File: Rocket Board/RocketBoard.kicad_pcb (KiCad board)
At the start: 2 copper layers, 52 parts, among them P1 PA_8, P10 PB_5, P11 PC_9, P12 PC_8, P13 PC_0, P14 PC_1, P15 PC_2, P16 PC_3, P17 CONN_01X04, P18 I2C, P19 Power, P2 PA_9, P3 PA_10, P4 PA_11, P5 PB_2, P6 PB_1, P7 PC_5, P8 PC_4, P9 PB_4, SW1 SPST, U1 STM32F401RCT6, U2 LD1117S33TR, Y1 25MHz

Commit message: Partial Layout of Board
Started the board layout process
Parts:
- added REF**: MountingHole_3.5mm_Pad, Mounting_Holes:MountingHole_3.5mm_Pad, F.Cu at (105.7, 100.3)
- added REF**: MountingHole_2.5mm_Pad, Mounting_Holes:MountingHole_2.5mm_Pad, F.Cu at (103.9, 120.9)
- C1, C10, C2, C3, C4, C5, C6, C7, C9: moved to B.Cu
- SWD: renamed from P17; value CONN_01X04 -> SWD
- Status 1: renamed from D2
- Status 2: renamed from D3
- moved P3 139.7 mm to (176.5, 95.2), turned to 90 degrees
- moved P15 131.8 mm to (176.5, 107.4), turned to 90 degrees
- moved P14 130.7 mm to (176.5, 104.4), turned to 90 degrees
- moved P13 129.7 mm to (176.5, 101.3), turned to 90 degrees
- moved P4 128.7 mm to (176.5, 98.3), turned to 90 degrees
- moved P1 127.3 mm to (176.5, 89.2), turned to 90 degrees
- moved P12 125.5 mm to (176.5, 86.1), turned to 90 degrees
- moved P11 124.9 mm to (176.5, 83.1), turned to 90 degrees
- moved P10 124.3 mm to (176.5, 80.0), turned to 90 degrees
- moved RP1 119.6 mm to (168.4, 93.7)
- moved C7 109.7 mm to (153.7, 91.7), turned to 90 degrees
- moved C2 99.8 mm to (143.0, 103.9)
- moved C4 99.8 mm to (142.0, 92.5), turned to 90 degrees
- moved C3 97.7 mm to (143.5, 98.0), turned to 90 degrees
- moved R4 96.8 mm to (148.1, 81.5)
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- renumbered D1 to PWR
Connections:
- RP1 pad 1: /PA_8 -> /PA_11
- RP1 pad 2: /PA_9 -> /PA_10
- RP1 pad 3: /PA_10 -> /PA_9
- RP1 pad 4: /PA_11 -> /PA_8
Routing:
- net GND: track 0.00 -> 43.7 mm, vias 0 -> 3
- net +3V3: track 0.00 -> 21.9 mm, vias 0 -> 3
- net /NRST: track 0.00 -> 10.8 mm
- net Net-(D3-Pad2): track 0.00 -> 9.67 mm
- net Net-(D2-Pad2): track 0.00 -> 9.67 mm
- net /PC_4: track 0.00 -> 9.41 mm
- net /OSC2: track 0.00 -> 9.11 mm, vias 0 -> 2
- net /PC_5: track 0.00 -> 8.77 mm
- net /PB_1: track 0.00 -> 8.19 mm
- net /PA_1: track 0.00 -> 7.99 mm
- net +12V: track 0.00 -> 7.91 mm
- net /PB_2: track 0.00 -> 7.84 mm
- net /OSC1: track 0.00 -> 7.74 mm
- net Net-(C15-Pad2): track 0.00 -> 6.19 mm
- net /PA_0: track 0.00 -> 5.78 mm
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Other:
- board outline added: 64.5 x 40.9 mm
- rule trace_min: 0.2 -> 0.1

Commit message: Finish Layout
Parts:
- removed the REF** at (105.7, 100.3)
- added MAV3: MAVRIC, Labels:MAVRIC, B.Cu at (132.8, 91.7)
- R3, R4: moved to B.Cu
- moved REF** 50.7 mm to (153.7, 111.5)
- moved R3 7.45 mm to (140.9, 81.5), turned to 270 degrees
- moved P1 6.87 mm to (169.7, 89.5)
- moved P12 6.87 mm to (169.7, 86.5)
- moved P15 6.87 mm to (169.7, 107.8)
- moved P16 6.87 mm to (169.7, 110.8)
- moved P10 6.87 mm to (169.7, 80.4)
- moved P11 6.87 mm to (169.7, 83.4)
- moved P13 6.87 mm to (169.7, 101.7)
- moved P14 6.87 mm to (169.7, 104.7)
- moved P2 6.87 mm to (169.7, 92.6)
- moved P3 6.87 mm to (169.7, 95.6)
- moved P4 6.87 mm to (169.7, 98.7)
- moved P9 6.87 mm to (169.7, 77.3)
- moved RP1 6.87 mm to (161.5, 94.1)
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- renumbered P18 to I2C
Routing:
- net GND: track 43.7 -> 93.0 mm, vias 3 -> 17
- net /PC_3: track 0.00 -> 29.7 mm, vias 0 -> 2
- net /PC_2: track 0.00 -> 28.5 mm, vias 0 -> 2
- net /PC_1: track 0.00 -> 26.9 mm, vias 0 -> 2
- net Net-(P8-Pad1): track 0.00 -> 26.5 mm
- net /PB_5: track 0.00 -> 26.1 mm
- net /PC_0: track 0.00 -> 25.9 mm, vias 0 -> 2
- net Net-(P7-Pad1): track 0.00 -> 25.7 mm
- net /PC_8: track 0.00 -> 24.2 mm, vias 0 -> 2
- net /PC_9: track 0.00 -> 23.9 mm, vias 0 -> 2
- net Net-(P6-Pad1): track 0.00 -> 23.6 mm
- net /SCL_1: track 0.00 -> 23.0 mm, vias 0 -> 1
- net +3V3: track 21.9 -> 43.5 mm, vias 3 -> 5
- net /NRST: track 10.8 -> 31.7 mm, vias 0 -> 1
- net /SDA_1: track 0.00 -> 20.4 mm, vias 0 -> 1
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- added copper zone on F.Cu, net +3V3
- added copper zone on B.Cu, net GND
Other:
- board size 64.5 x 40.9 mm -> 58.5 x 40.9 mm
- board text added: "M A V R I C Main Board"

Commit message: Fix analog input, Add 2 UART ports, changed PWM1/3 to PWM1/3N
Removed the series resistors for analog inputs, added pinouts for
UART1,2.   Changed PWM 1/3 tp PWM 1/3N to free up RX1 pin
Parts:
- removed P13: PC_0, Pin_Headers:Pin_Header_Straight_1x02
- removed P14: PC_1, Pin_Headers:Pin_Header_Straight_1x02
- removed P15: PC_2, Pin_Headers:Pin_Header_Straight_1x02
- removed P16: PC_3, Pin_Headers:Pin_Header_Straight_1x02
- removed REF**: MountingHole_2.5mm_Pad, Mounting_Holes:MountingHole_2.5mm_Pad
- removed RP4: 220 4pack, Resistors_SMD:R_Array_Convex_4x1206
- added PC0: PC_0, Pin_Headers:Pin_Header_Straight_1x02, F.Cu at (169.7, 101.8)
- added PC1: PC_1, Pin_Headers:Pin_Header_Straight_1x02, F.Cu at (169.7, 104.9)
- added PC2: PC_2, Pin_Headers:Pin_Header_Straight_1x02, F.Cu at (169.7, 108.0)
- added PC3: PC_3, Pin_Headers:Pin_Header_Straight_1x02, F.Cu at (169.7, 111.0)
- added UART1: UART1, Pin_Headers:Pin_Header_Straight_1x02, F.Cu at (153.8, 110.8)
- added UART2: UART2, Pin_Headers:Pin_Header_Straight_1x02, F.Cu at (159.4, 110.9)
- renumbered P3 to PA10, P4 to PA11, P1 to PA8, P2 to PA9, P6 to PB1, P5 to PB2, P9 to PB4, P10 to PB5, P8 to PC4, P7 to PC5, P12 to PC8, P11 to PC9
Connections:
- RP1 pad 1: /PA_11 -> /PB_15
- RP1 pad 2: /PA_10 -> /PA_11
- U1 pad 16: GND -> /TX2
- U1 pad 17: GND -> /RX2
- U1 pad 36: GND -> /PB_15
- U1 pad 43: /PA_10 -> /RX1
- U1 pad 58: GND -> /TX1
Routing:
- net /RX2: track 0.00 -> 37.9 mm
- net /TX2: track 0.00 -> 37.8 mm
- net /TX1: track 0.00 -> 26.3 mm
- net +3V3: track 43.5 -> 65.3 mm, vias 5 -> 9
- net /RX1: track 0.00 -> 17.9 mm
- net /PB_15: track 0.00 -> 17.8 mm
- net /PC_3: track 29.7 -> 40.4 mm
- net (no net): track 0.00 -> 10.2 mm, vias 0 -> 2
- net /PC_2: track 28.5 -> 37.7 mm
- net /PA_10: track 8.79 -> 0.00 mm
- net /PC_1: track 26.9 -> 35.1 mm
- net /PC_0: track 25.9 -> 33.7 mm
- net Net-(P13-Pad1): track 7.69 -> 0.00 mm
- net Net-(P16-Pad1): track 7.69 -> 0.00 mm
- net Net-(P15-Pad1): track 6.99 -> 0.00 mm
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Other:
- board text added: "Analog"
- board text added: "GND"
- board text added: "M A V R I C Danny Mallek 2016"
- board text added: "Main Board Rev2.0"
- board text removed: "M A V R I C Main Board"

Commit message: Fix power distribution issues on main board, initial soil board commit
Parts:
- renumbered P19 to PWR
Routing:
- net +3V3: track 65.3 -> 91.7 mm, vias 9 -> 12
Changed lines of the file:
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@@
   (general
     (links 142)
-    (no_connects 8)
+    (no_connects 5)
     (area 116.764999 74.346999 175.385801 115.391001)
     (thickness 1.6)
     (drawings 15)
-    (tracks 511)
+    (tracks 533)
     (zones 0)
     (modules 54)
@@
     (descr "Through hole pin header")
     (tags "pin header")
-    (fp_text reference P19 (at 0.0508 4.9784) (layer F.SilkS)
+    (fp_text reference PWR (at 0.0508 4.9784) (layer F.SilkS)
       (effects (font (size 1 1) (thickness 0.15)))
     )
@@
   (segment (start 145.4404 113.6396) (end 144.4244 112.6236) (width 0.4) (layer B.Cu) (net 0))
   (via (at 145.4404 113.6396) (size 0.8) (drill 0.6) (layers F.Cu B.Cu) (net 0))
+  (segment (start 127.762 84.836) (end 129.54 86.614) (width 0.75) (layer F.Cu) (net 1))
+  (via (at 129.54 86.614) (size 0.8) (drill 0.6) (layers F.Cu B.Cu) (net 1))
+  (segment (start 127.73 84.614) (end 129.54 82.804) (width 0.75) (layer F.Cu) (net 1))
+  (via (at 129.54 82.804) (size 0.8) (drill 0.6) (layers F.Cu B.Cu) (net 1))
   (segment (start 144.546 89.55) (end 144.546 88.2196) (width 0.25) (layer F.Cu) (net 1))
   (via (at 145.2372 87.4268) (size 0.6) (drill 0.4) (layers F.Cu B.Cu) (net 1))
@@
   (segment (start 133.506 75.978) (end 140.306 75.978) (width 0.2) (layer F.Cu) (net 1))
   (segment (start 127.73 84.836) (end 127.73 84.614) (width 0.75) (layer F.Cu) (net 1))
-  (segment (start 127.73 84.614) (end 129.54 82.804) (width 0.75) (layer F.Cu) (net 1))
-  (via (at 129.54 82.804) (size 0.8) (drill 0.6) (layers F.Cu B.Cu) (net 1))
   (segment (start 127.73 84.836) (end 127.762 84.836) (width 0.75) (layer F.Cu) (net 1))
-  (segment (start 127.762 84.836) (end 129.54 86.614) (width 0.75) (layer F.Cu) (net 1))
-  (via (at 129.54 86.614) (size 0.8) (drill 0.6) (layers F.Cu B.Cu) (net 1))
   (segment (start 127.73 84.836) (end 130.048 84.836) (width 0.75) (layer F.Cu) (net 1))
   (via (at 130.048 84.836) (size 0.8) (drill 0.6) (layers F.Cu B.Cu) (net 1))
@@
   (segment (start 129.032 88.646) (end 130.302 87.376) (width 0.25) (layer F.Cu) (net 1))
   (segment (start 130.302 87.376) (end 132.908 87.376) (width 0.25) (layer F.Cu) (net 1))
+  (segment (start 149.86 102.616) (end 153.6192 102.616) (width 0.25) (layer B.Cu) (net 2))
+  (via (at 155.4988 104.4956) (size 0.6) (drill 0.4) (layers F.Cu B.Cu) (net 2))
+  (segment (start 153.6192 102.616) (end 155.4988 104.4956) (width 0.25) (layer B.Cu) (net 2))
+  (segment (start 144.4244 90.7796) (end 144.905602 90.7796) (width 0.25) (layer F.Cu) (net 2))
+  (via (at 148.2852 91.5416) (size 0.6) (drill 0.4) (layers F.Cu B.Cu) (net 2))
+  (segment (start 147.4724 91.5416) (end 148.2852 91.5416) (width 0.25) (layer B.Cu) (net 2))
+  (segment (start 146.304 92.71) (end 147.4724 91.5416) (width 0.25) (layer B.Cu) (net 2))
+  (via (at 146.304 92.71) (size 0.6) (drill 0.4) (layers F.Cu B.Cu) (net 2))
+  (segment (start 146.304 92.177998) (end 146.304 92.71) (width 0.25) (layer F.Cu) (net 2))
+  (segment (start 144.905602 90.7796) (end 146.304 92.177998) (width 0.25) (layer F.Cu) (net 2))
+  (via (at 149.86 102.616) (size 0.6) (drill 0.4) (layers F.Cu B.Cu) (net 2))
+  (segment (start 149.86 102.616) (end 149.794 102.682) (width 0.15) (layer B.Cu) (net 2))
+  (segment (start 149.794 102.682) (end 149.794 103.886) (width 0.15) (layer B.Cu) (net 2))
+  (segment (start 143.046 100.95) (end 143.046 102.8632) (width 0.25) (layer F.Cu) (net 2))
+  (segment (start 143.0528 102.87) (end 143.952 103.7692) (width 0.25) (layer B.Cu) (net 2))
+  (via (at 143.0528 102.87) (size 0.6) (drill 0.4) (layers F.Cu B.Cu) (net 2))
+  (segment (start 143.046 102.8632) (end 143.0528 102.87) (width 0.25) (layer F.Cu) (net 2))
+  (segment (start 143.952 103.7692) (end 143.952 103.886) (width 0.25) (layer B.Cu) (net 2))
+  (segment (start 143.952 103.886) (end 145.5928 103.886) (width 0.25) (layer B.Cu) (net 2))
+  (segment (start 149.794 106.1872) (end 149.794 103.886) (width 0.25) (layer B.Cu) (net 2))
+  (segment (start 149.3012 106.68) (end 149.794 106.1872) (width 0.25) (layer B.Cu) (net 2))
+  (segment (start 147.2184 106.68) (end 149.3012 106.68) (width 0.25) (layer B.Cu) (net 2))
+  (segment (start 146.4056 105.8672) (end 147.2184 106.68) (width 0.25) (layer B.Cu) (net 2))
+  (segment (start 146.4056 104.6988) (end 146.4056 105.8672) (width 0.25) (layer B.Cu) (net 2))
+  (segment (start 145.5928 103.886) (end 146.4056 104.6988) (width 0.25) (layer B.Cu) (net 2))
+  (segment (start 141.224 91.44) (end 141.224 90.678) (width 0.25) (layer F.Cu) (net 2))
+  (segment (start 140.5636 90.0176) (end 140.3096 90.0176) (width 0.25) (layer F.Cu) (net 2))
+  (segment (start 141.224 90.678) (end 140.5636 90.0176) (width 0.25) (layer F.Cu) (net 2))
+  (segment (start 151.496 91.5) (end 152.4416 91.5) (width 0.25) (layer F.Cu) (net 2))
+  (segment (start 153.162 90.7796) (end 153.5684 90.7796) (width 0.25) (layer F.Cu) (net 2))
+  (segment (start 152.4416 91.5) (end 153.162 90.7796) (width 0.25) (layer F.Cu) (net 2))
   (segment (start 155.702 90.744) (end 157.3428 90.744) (width 0.25) (layer B.Cu) (net 2))
   (via (at 157.3784 90.7796) (size 0.6) (drill 0.4) (layers F.Cu B.Cu) (net 2))
@@
   (segment (start 120.566 103.632) (end 120.566 100.33) (width 0.25) (layer F.Cu) (net 2))
   (segment (start 149.546 100.95) (end 149.546 102.302) (width 0.15) (layer F.Cu) (net 2))
-  (segment (start 149.794 102.682) (end 149.794 103.886) (width 0.15) (layer B.Cu) (net 2))
-  (segment (start 149.86 102.616) (end 149.794 102.682) (width 0.15) (layer B.Cu) (net 2))
-  (via (at 149.86 102.616) (size 0.6) (drill 0.4) (layers F.Cu B.Cu) (net 2))
   (segment (start 149.546 102.302) (end 149.86 102.616) (width 0.15) (layer F.Cu) (net 2))
-  (segment (start 143.046 100.95) (end 143.046 102.318) (width 0.15) (layer F.Cu) (net 2))
-  (segment (start 143.952 103.312) (end 143.952 103.886) (width 0.15) (layer B.Cu) (net 2))
-  (segment (start 143.256 102.616) (end 143.952 103.312) (width 0.15) (layer B.Cu) (net 2))
-  (via (at 143.256 102.616) (size 0.6) (drill 0.4) (layers F.Cu B.Cu) (net 2))
-  (segment (start 143.256 102.528) (end 143.256 102.616) (width 0.15) (layer F.Cu) (net 2))
-  (segment (start 143.046 102.318) (end 143.256 102.528) (width 0.15) (layer F.Cu) (net 2))
   (segment (start 140.096 91.5) (end 141.164 91.5) (width 0.15) (layer F.Cu) (net 2))
   (segment (start 141.29 91.506) (end 141.986 91.506) (width 0.15) (layer B.Cu) (net 2))
@@
   (segment (start 154.8504 94.5) (end 155.092 94.7416) (width 0.25) (layer F.Cu) (net 29))
   (segment (start 147.046 100.95) (end 147.046 101.874) (width 0.15) (layer F.Cu) (net 30))
+  (segment (start 147.046 101.874) (end 145.542 103.378) (width 0.15) (layer F.Cu) (net 30))
+  (segment (start 145.542 103.378) (end 145.542 103.886) (width 0.15) (layer F.Cu) (net 30))
+  (segment (start 145.542 103.886) (end 143.002 106.426) (width 0.15) (layer F.Cu) (net 30))
+  (segment (start 143.002 106.426) (end 143.002 106.602) (width 0.15) (layer F.Cu) (net 30))
   (segment (start 143.002 106.602) (end 142.392 107.212) (width 0.15) (layer F.Cu) (net 30))
-  (segment (start 143.002 106.426) (end 143.002 106.602) (width 0.15) (layer F.Cu) (net 30))
-  (segment (start 145.542 103.886) (end 143.002 106.426) (width 0.15) (layer F.Cu) (net 30))
-  (segment (start 145.542 103.378) (end 145.542 103.886) (width 0.15) (layer F.Cu) (net 30))
-  (segment (start 147.046 101.874) (end 145.542 103.378) (width 0.15) (layer F.Cu) (net 30))
   (segment (start 141.072 107.212) (end 141.072 106.324) (width 0.15) (layer F.Cu) (net 31))
+  (segment (start 141.072 106.324) (end 144.272 103.124) (width 0.15) (layer F.Cu) (net 31))
+  (segment (start 144.272 103.124) (end 145.034 103.124) (width 0.15) (layer F.Cu) (net 31))
+  (segment (start 145.034 103.124) (end 146.046 102.112) (width 0.15) (layer F.Cu) (net 31))
   (segment (start 146.046 102.112) (end 146.046 100.95) (width 0.15) (layer F.Cu) (net 31))
-  (segment (start 145.034 103.124) (end 146.046 102.112) (width 0.15) (layer F.Cu) (net 31))
-  (segment (start 144.272 103.124) (end 145.034 103.124) (width 0.15) (layer F.Cu) (net 31))
-  (segment (start 141.072 106.324) (end 144.272 103.124) (width 0.15) (layer F.Cu) (net 31))
   (segment (start 143.732 107.212) (end 143.732 106.458) (width 0.15) (layer F.Cu) (net 32))
   (segment (start 147.546 101.882) (end 147.546 100.95) (width 0.15) (layer F.Cu) (net 32))

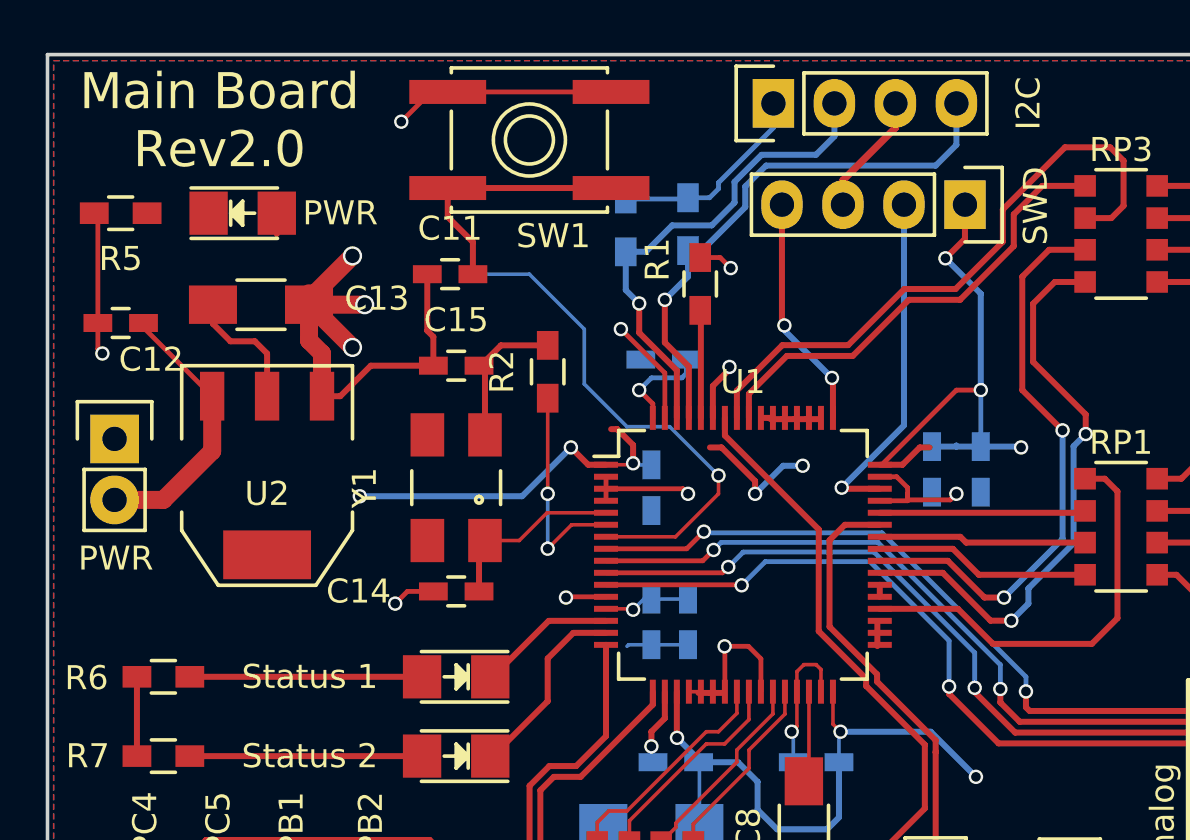
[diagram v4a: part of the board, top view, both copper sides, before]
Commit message: Create Analog Sensor Board, Add Conglomerate1 Board (Advanced Circuits Order)
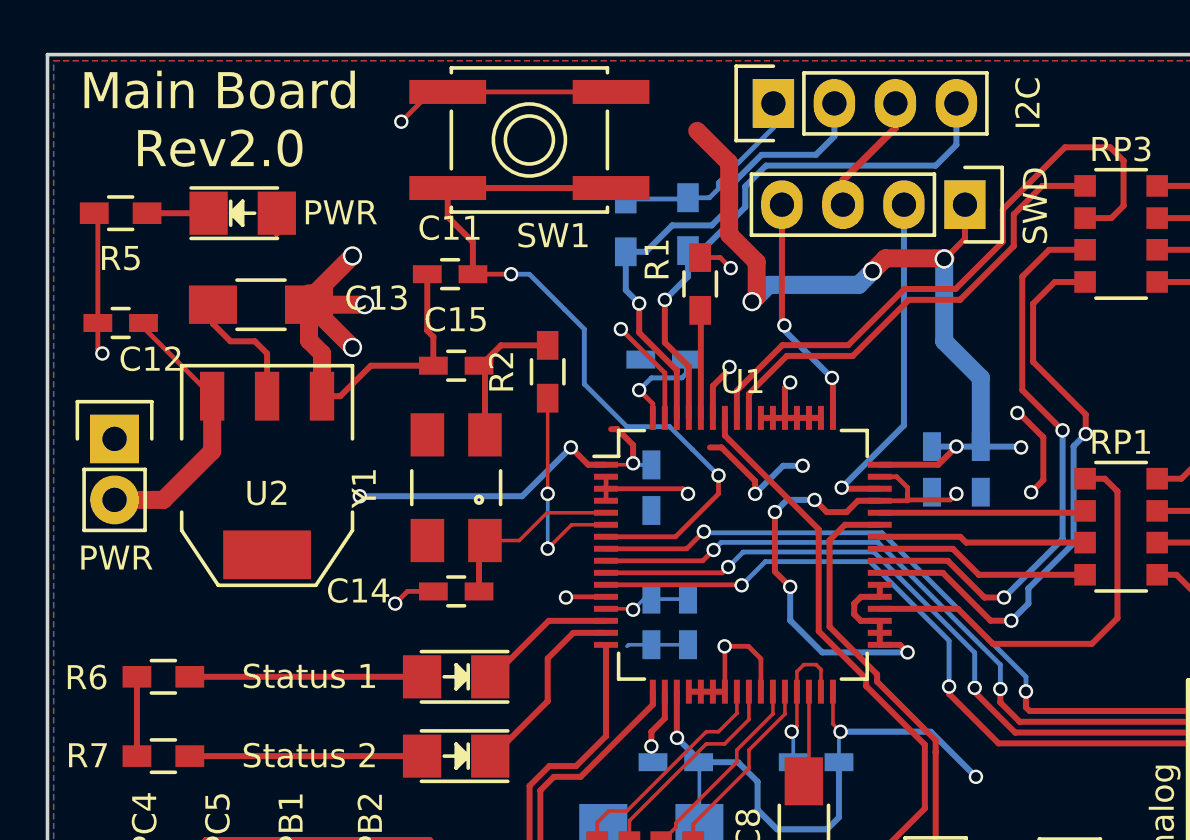
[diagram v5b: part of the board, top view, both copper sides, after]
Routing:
- net GND: track 86.7 -> 107.6 mm, vias 16 -> 21
- net (no net): track 10.2 -> 19.7 mm, vias 2 -> 6
- net +3V3: track 91.7 -> 99.1 mm
- net Net-(D1-Pad1): track 0.00 -> 2.56 mm
- net /NRST: track 31.7 -> 32.0 mm, vias 1 -> 2
